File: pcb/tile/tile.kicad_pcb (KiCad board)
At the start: 2 copper layers, 21.4 x 30.7 mm, 17 parts, among them IC1 THVD1420DR, J1 LED Strip, J2 UPDI, J5 12V, J6 RS-485 Jack, U1 ATtiny3224-X

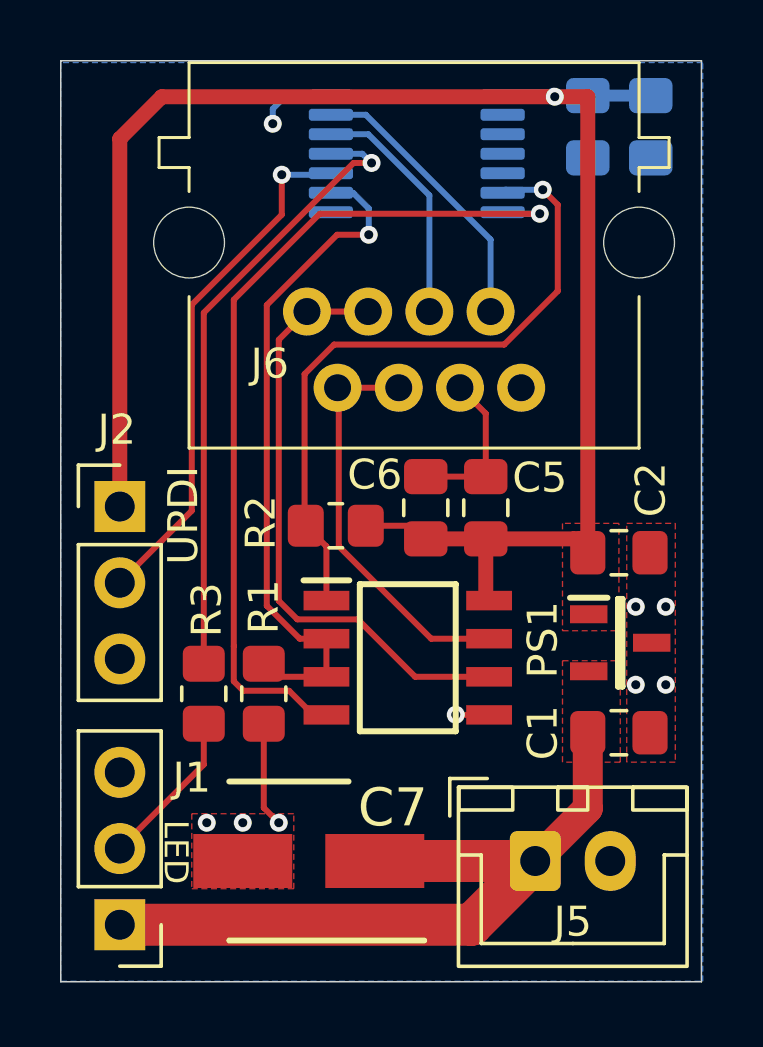
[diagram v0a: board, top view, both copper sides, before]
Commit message: pcb: 3.3V transceiver supply, second Row Bus chain, fab outputs
The THVD1420DR transceivers ran at VCC=5V while driving 3.3V-only GPIOs on
both boards. Per the datasheet the receiver output swings to VCC-0.4V min
(~4.6-4.8V at 5V), and the RX pull-ups went to 5V as well, so both the Pi's
and the RP2350's inputs sat out of spec. Both boards were bodged to 3.3V on
the bench; these schematics bring the sources in line.

pi-hat:
- IC3 supply, decoupling and RX pull-up moved from +5V to +3V3; no +5V net
  remains on the board.
- Second Row Bus chain added (IC4) so the 8 rows split across two chains -
  see docs/row-bus-protocol.md for why one chain no longer fits the frame
  budget. Chain A on uart0 (GPIO14/15), chain B on uart2 (GPIO4/5).
- Both direction lines moved onto the UARTs' own RTS pins, GPIO17 and
  GPIO7, so the kernel's RS-485 mode can eventually drive them with
  hardware timing instead of the host's busy-wait.
- Single RJ45 carries both chains on correctly-paired T568B conductors:
  chain A on pins 1-2, chain B on 3-6, grounds on the blue and brown pairs.

row-controller:
- Both transceivers, the INA220 and its I2C pull-ups moved to +3V3. +5V now
  only feeds the Xiao's VUSB input and the regulator that makes it.
- INA220 VBUS now senses +12V through the 5 mOhm shunt, matching what
  docs/row-bus-protocol.md's POWER command has always claimed it measures;
  it previously sat on the 5V rail and reported ~4.8V.

Also adds v1.0/1.2 gerbers and BOM CSVs, following the existing
gerber-1.1 pattern.

Reviewed the pi-hat netlist in detail - header pins, transceiver
orientation, rails, termination and pairing all check out. The
row-controller and tile changes are carried as-is.

Co-Authored-By: Claude Opus 5 <noreply@anthropic.com>
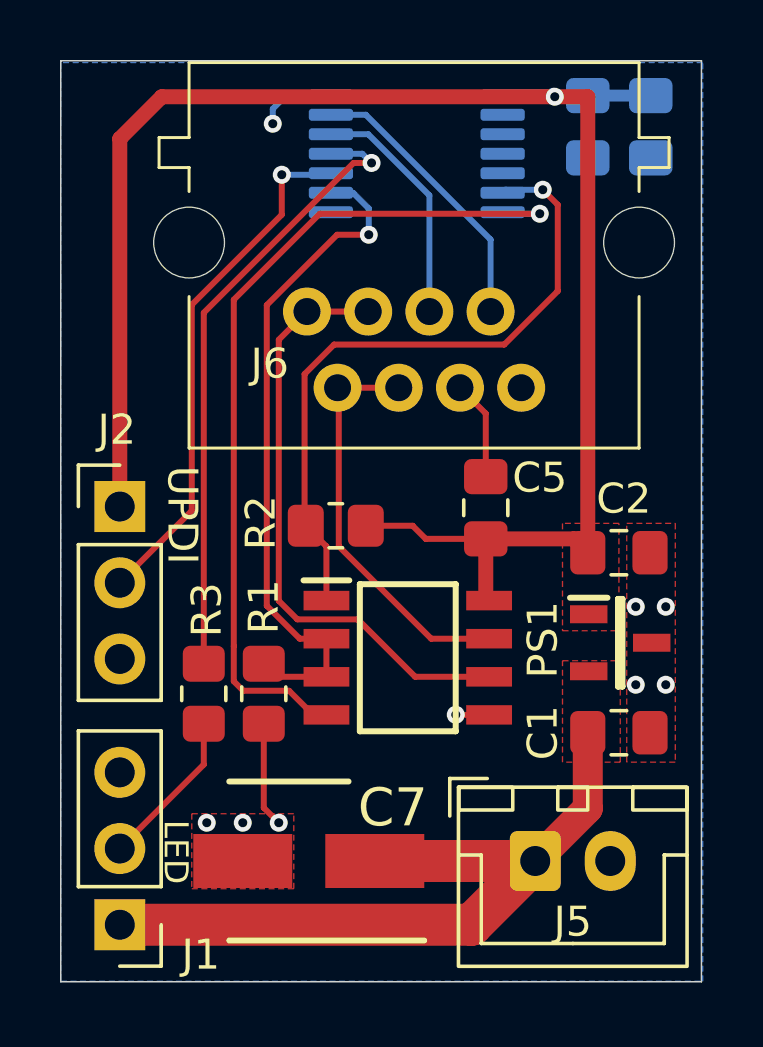
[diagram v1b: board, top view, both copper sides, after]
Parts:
- removed C6: 100nF, Capacitor_SMD:C_0805_2012Metric_Pad1.18x1.45mm_HandSolder
- C5: value 100nF -> 0.1uF
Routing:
- net GND: track 12.6 -> 10.6 mm
